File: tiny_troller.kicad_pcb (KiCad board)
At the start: 4 copper layers, 11.1 x 11.4 mm, 30 parts, among them U1 MA702GQ-P, U3 STM32G071G8U6, U5 MCP2025-330E_MD, U6 MAX14870ETC+T

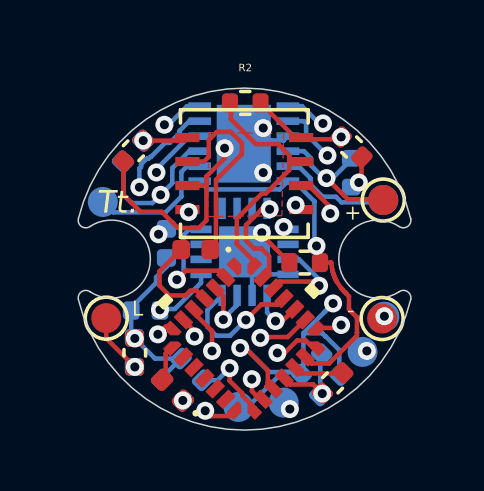
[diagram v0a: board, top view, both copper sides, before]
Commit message: R5 added, circuitry for MCP2025 LIN transceiver and regulator VBB pin should be correct now.
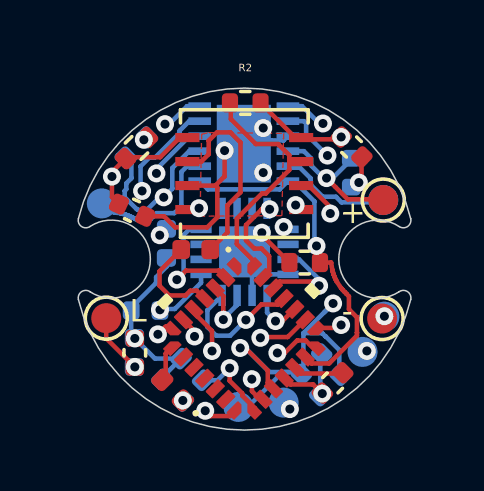
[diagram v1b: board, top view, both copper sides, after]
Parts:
- added R5: R_Small, Resistor_SMD:R_0402_1005Metric, F.Cu at (159.6, 101.5)
- R2: value R_Small_US -> R_Small
- moved C5 1.98 mm to (159.4, 103.6), turned to 155 degrees
- moved D2 0.16 mm to (159.5, 101.5), turned to 224 degrees
- moved TP10 0.06 mm to (158.4, 103.3)
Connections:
- D2 pad 1: Net-(C5-Pad2) -> Net-(D2-Pad1)
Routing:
- net Net-(C5-Pad2): track 5.54 -> 7.21 mm
- net GND: track 24.1 -> 22.6 mm
- net DRV_ENABLE: track 16.5 -> 15.2 mm
- net PWR: track 20.4 -> 21.6 mm
- net DRV_PWM: track 15.8 -> 16.8 mm
- net LBUS: track 8.63 -> 9.20 mm
- net Net-(D2-Pad1): vias 0 -> 1
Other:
- board text added: ".01"
- board text removed: ".00"

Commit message: v01 design first pass done (all components selected for the first time).
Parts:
- added C3: 100n, Capacitor_SMD:C_0402_1005Metric, F.Cu at (162.2, 100.0)
- C5: value C_Small -> 22u
- C6: value C_Small -> 10u
- D4: value D_Zener_Small -> CPDQC24VEU-HF
- D5: value D_TVS -> CPDQR24V-HF
- R2: value R_Small -> 10k
- moved R2 0.93 mm to (164.1, 100.0), turned to 350 degrees
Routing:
- net GND: track 22.6 -> 23.8 mm
- net Net-(C3-Pad2): track 6.56 -> 7.63 mm
- net LIN_RESET: track 8.07 -> 7.31 mm
- net +3V3: track 35.9 -> 35.3 mm
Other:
- board text added: "MAKE SURE THESE ARENT GONNA SHORt ON GND PAD..."

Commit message: included the final v00 BOM
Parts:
- D2, D3: value D_Small -> CLS10F40,L3F
- R3: value R_Small_US -> 70m
- R4: value R_Small_US -> 10k
- R5: value R_Small -> 2
- renumbered C13 to C8, C14 to C9
